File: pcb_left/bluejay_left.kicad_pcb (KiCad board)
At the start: 2 copper layers, 0 parts

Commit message: Work on PCBs
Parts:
- added C1: 22p, BlueJay footprints:C_Disc_D3.0mm_W1.6mm_P2.50mm, F.Cu at (191.0, 76.2)
- added C2: 22p, BlueJay footprints:C_Disc_D3.0mm_W1.6mm_P2.50mm, F.Cu at (191.0, 90.8)
- added C3: 4.7u, BlueJay footprints:CP_Radial_D4.0mm_P1.50mm, F.Cu at (201.8, 45.0)
- added C4: 100n, BlueJay footprints:C_Disc_D4.3mm_W1.9mm_P5.00mm, F.Cu at (193.2, 74.0)
- added C5: 100n, BlueJay footprints:C_Disc_D4.3mm_W1.9mm_P5.00mm, F.Cu at (206.8, 82.2)
- added DZ1: 3.6V, Diode_THT_AKL:D_DO-35_SOD27_P7.62mm_Horizontal_Zener, F.Cu at (167.0, 26.0)
- added DZ2: 3.6V, Diode_THT_AKL:D_DO-35_SOD27_P7.62mm_Horizontal_Zener, F.Cu at (172.8, 26.1)
- added Da1: 1N4148, Diode_THT_AKL:D_DO-35_SOD27_P7.62mm_Horizontal, F.Cu at (203.4, 107.2)
- added Da2: 1N4148, Diode_THT_AKL:D_DO-35_SOD27_P7.62mm_Horizontal, F.Cu at (203.4, 114.3)
- added Da3: 1N4148, Diode_THT_AKL:D_DO-35_SOD27_P7.62mm_Horizontal, F.Cu at (196.2, 140.5)
- added Da4: 1N4148, Diode_THT_AKL:D_DO-35_SOD27_P7.62mm_Horizontal, F.Cu at (203.4, 121.4)
- added Da5: 1N4148, Diode_THT_AKL:D_DO-35_SOD27_P7.62mm_Horizontal, F.Cu at (203.4, 133.3)
- added Db1: 1N4148, Diode_THT_AKL:D_DO-35_SOD27_P7.62mm_Horizontal, F.Cu at (191.5, 121.4)
- added Db2: 1N4148, Diode_THT_AKL:D_DO-35_SOD27_P7.62mm_Horizontal, F.Cu at (191.5, 114.3)
- added Db3: 1N4148, Diode_THT_AKL:D_DO-35_SOD27_P7.62mm_Horizontal, F.Cu at (191.5, 107.2)
- added Db4: 1N4148, Diode_THT_AKL:D_DO-35_SOD27_P7.62mm_Horizontal, F.Cu at (193.8, 126.2)
- added Db5: 1N4148, Diode_THT_AKL:D_DO-35_SOD27_P7.62mm_Horizontal, F.Cu at (191.5, 131.0)
- added Dc1: 1N4148, Diode_THT_AKL:D_DO-35_SOD27_P7.62mm_Horizontal, F.Cu at (179.5, 114.3)
- added Dc2: 1N4148, Diode_THT_AKL:D_DO-35_SOD27_P7.62mm_Horizontal, F.Cu at (181.9, 107.2)
- added Dc3: 1N4148, Diode_THT_AKL:D_DO-35_SOD27_P7.62mm_Horizontal, F.Cu at (179.5, 121.4)
- added Dc4: 1N4148, Diode_THT_AKL:D_DO-35_SOD27_P7.62mm_Horizontal, F.Cu at (181.9, 102.4)
- added Dc5: 1N4148, Diode_THT_AKL:D_DO-35_SOD27_P7.62mm_Horizontal, F.Cu at (179.5, 128.6)
- added Dd1: 1N4148, Diode_THT_AKL:D_DO-35_SOD27_P7.62mm_Horizontal, F.Cu at (108.1, 31.0)
- added Dd2: 1N4148, Diode_THT_AKL:D_DO-35_SOD27_P7.62mm_Horizontal, F.Cu at (117.6, 19.1)
- added Dd3: 1N4148, Diode_THT_AKL:D_DO-35_SOD27_P7.62mm_Horizontal, F.Cu at (108.1, 26.2)
- added Dd4: 1N4148, Diode_THT_AKL:D_DO-35_SOD27_P7.62mm_Horizontal, F.Cu at (105.7, 21.4)
- added Dd5: 1N4148, Diode_THT_AKL:D_DO-35_SOD27_P7.62mm_Horizontal, F.Cu at (105.4, 14.3)
- added De1: 1N4148, Diode_THT_AKL:D_DO-35_SOD27_P7.62mm_Horizontal, F.Cu at (89.1, 42.9)
- added De2: 1N4148, Diode_THT_AKL:D_DO-35_SOD27_P7.62mm_Horizontal, F.Cu at (89.1, 35.7)
- added De3: 1N4148, Diode_THT_AKL:D_DO-35_SOD27_P7.62mm_Horizontal, F.Cu at (91.4, 31.0)
- added De4: 1N4148, Diode_THT_AKL:D_DO-35_SOD27_P7.62mm_Horizontal, F.Cu at (91.4, 23.8)
- added Df2: 1N4148, Diode_THT_AKL:D_DO-35_SOD27_P7.62mm_Horizontal, F.Cu at (70.0, 52.4)
- added Df3: 1N4148, Diode_THT_AKL:D_DO-35_SOD27_P7.62mm_Horizontal, F.Cu at (70.0, 42.9)
- added Df4: 1N4148, Diode_THT_AKL:D_DO-35_SOD27_P7.62mm_Horizontal, F.Cu at (70.0, 35.7)
- added F1: 100mA, BlueJay footprints:polyfuse_5.1mm, F.Cu at (204.0, 35.7)
- added J1: SJ-43514, BlueJay footprints:CUI_SJ-43514, F.Cu at (195.3, 23.8)
- added PB1: RESET, BlueJay footprints:SW_PUSH_6mm, F.Cu at (149.0, 19.0)
- added PB2: BOOT, BlueJay footprints:SW_PUSH_6mm, F.Cu at (137.0, 19.0)
- added R1: 1.5k, BlueJay footprints:R_Axial_DIN0204_L3.6mm_D1.6mm_P5.08mm_Horizontal, F.Cu at (200.5, 55.8)
- added R2: 75R, BlueJay footprints:R_Axial_DIN0204_L3.6mm_D1.6mm_P5.08mm_Horizontal, F.Cu at (191.2, 55.7)
- added R3: 75R, BlueJay footprints:R_Axial_DIN0204_L3.6mm_D1.6mm_P5.08mm_Horizontal, F.Cu at (196.0, 55.7)
- added R4: 10k, BlueJay footprints:R_Axial_DIN0204_L3.6mm_D1.6mm_P5.08mm_Horizontal, F.Cu at (161.5, 23.5)
- added SWa1: KEYSW, BlueJay footprints:Kailh_socket_MX, F.Cu at (169.1, 47.6)
- added SWa2: KEYSW, BlueJay footprints:Kailh_socket_MX, F.Cu at (169.1, 66.7)
- added SWa3: KEYSW, BlueJay footprints:Kailh_socket_MX, F.Cu at (169.1, 85.7)
- added SWa4: KEYSW, BlueJay footprints:Kailh_socket_MX, F.Cu at (169.1, 104.8)
- added SWa5: KEYSW, BlueJay footprints:Kailh_socket_MX, F.Cu at (198.2, 154.4)
- added SWb1: KEYSW, BlueJay footprints:Kailh_socket_MX, F.Cu at (150.0, 45.2)
- added SWb2: KEYSW, BlueJay footprints:Kailh_socket_MX, F.Cu at (150.0, 64.3)
- added SWb3: KEYSW, BlueJay footprints:Kailh_socket_MX, F.Cu at (150.0, 83.3)
- added SWb4: KEYSW, BlueJay footprints:Kailh_socket_MX, F.Cu at (150.0, 102.4)
- added SWb5: KEYSW, BlueJay footprints:Kailh_socket_MX, F.Cu at (181.3, 141.2)
- added SWc1: KEYSW, BlueJay footprints:Kailh_socket_MX, F.Cu at (131.0, 38.1)
- added SWc2: KEYSW, BlueJay footprints:Kailh_socket_MX, F.Cu at (131.0, 57.1)
- added SWc3: KEYSW, BlueJay footprints:Kailh_socket_MX, F.Cu at (130.7, 76.2)
- added SWc4: KEYSW, BlueJay footprints:Kailh_socket_MX, F.Cu at (131.0, 95.2)
- added SWc5: KEYSW, BlueJay footprints:Kailh_socket_MX, F.Cu at (161.7, 132.4)
- added SWd1: KEYSW, BlueJay footprints:Kailh_socket_MX, F.Cu at (111.9, 45.2)
- added SWd2: KEYSW, BlueJay footprints:Kailh_socket_MX, F.Cu at (111.9, 64.3)
- added SWd3: KEYSW, BlueJay footprints:Kailh_socket_MX, F.Cu at (111.9, 83.3)
- added SWd4: KEYSW, BlueJay footprints:Kailh_socket_MX, F.Cu at (111.9, 102.4)
- added SWd5: KEYSW, BlueJay footprints:Kailh_socket_MX, F.Cu at (140.5, 128.6)
- added SWe1: KEYSW, BlueJay footprints:Kailh_socket_MX, F.Cu at (92.9, 52.4)
- added SWe2: KEYSW, BlueJay footprints:Kailh_socket_MX, F.Cu at (92.9, 71.4)
- added SWe3: KEYSW, BlueJay footprints:Kailh_socket_MX, F.Cu at (92.9, 90.5)
- added SWe4: KEYSW, BlueJay footprints:Kailh_socket_MX, F.Cu at (92.7, 109.9)
- added SWf2: KEYSW, BlueJay footprints:Kailh_socket_MX, F.Cu at (73.5, 71.4)
- added SWf3: KEYSW, BlueJay footprints:Kailh_socket_MX, F.Cu at (73.8, 90.5)
- added SWf4: KEYSW, BlueJay footprints:Kailh_socket_MX, F.Cu at (73.8, 109.5)
- added U1: ATmega328P-PU, Package_DIP_AKL:DIP-28_W7.62mm_Socket, F.Cu at (196.2, 62.1)
- added USB1: USB_B_Mini, BlueJay footprints:USB_Mini_B_Female_548190519, F.Cu at (181.0, 27.5)
- added Y1: 16MHz, BlueJay footprints:Crystal_HC49-4H_Vertical, F.Cu at (191.8, 86.0)
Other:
- board outline added: 17.2 x 1.3 mm

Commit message: Further work on pcbs
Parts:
- DZ1, DZ2: footprint Diode_THT_AKL:D_DO-35_SOD27_P7.62mm_Horizontal_Zener -> BlueJay footprints:D_DO-35_SOD27_P5.08mm_Horizontal
- Da1, Da2, Da3, Da4, Da5, Db1, Db2, Db3, Db4, Db5, Dc1, Dc2, Dc3, Dc4, Dc5, Dd1, Dd2, Dd3, Dd4, Dd5, De1, De2, De3, De4, Df2, Df3, Df4: footprint Diode_THT_AKL:D_DO-35_SOD27_P7.62mm_Horizontal -> BlueJay footprints:D_DO-35_SOD27_P5.08mm_Horizontal
- moved Df4 19.0 mm to (77.3, 53.2), turned to 180 degrees
- moved Df3 16.5 mm to (78.6, 57.0), turned to 180 degrees
- moved Df2 13.3 mm to (80.3, 60.8), turned to 180 degrees
- moved Dd2 12.7 mm to (117.1, 31.8), turned to 180 degrees
- moved De4 11.3 mm to (96.2, 34.0), turned to 180 degrees
- moved Dd1 10.6 mm to (117.8, 35.2), turned to 180 degrees
- moved De1 10.5 mm to (99.6, 42.2), turned to 180 degrees
- moved De2 9.94 mm to (98.2, 39.5), turned to 180 degrees
- moved De3 8.21 mm to (97.2, 36.8), turned to 180 degrees
- turned Dd3 to 180 degrees
- turned Dd4 to 180 degrees
- turned Dd5 to 180 degrees

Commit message: Further PCB updates
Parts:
- moved Dc4 30.0 mm to (207.1, 118.8), turned to 180 degrees
- moved Dc3 27.7 mm to (206.3, 114.2), turned to 180 degrees
- moved Dc1 25.2 mm to (203.1, 105.2), turned to 180 degrees
- moved Da3 24.6 mm to (188.8, 117.0), turned to 180 degrees
- moved Dc2 22.8 mm to (204.6, 109.8), turned to 180 degrees
- moved Da1 18.4 mm to (185.1, 109.5), turned to 180 degrees
- moved Dd5 17.2 mm to (108.1, 31.2)
- moved Da2 16.8 mm to (186.6, 113.0), turned to 180 degrees
- moved Db1 16.5 mm to (192.3, 105.0), turned to 180 degrees
- moved Dd4 13.9 mm to (109.8, 34.8)
- moved C3 13.4 mm to (190.0, 51.5)
- moved Dc5 12.7 mm to (191.8, 125.2), turned to 180 degrees
- moved Da4 12.5 mm to (190.8, 121.0), turned to 180 degrees
- moved Da5 12.5 mm to (199.3, 121.5), turned to 180 degrees
- moved F1 11.9 mm to (196.0, 44.5)
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
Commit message: Further work on pcbs
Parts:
- F1: footprint BlueJay footprints:polyfuse_5.1mm -> Fuse_AKL:Fuse_Bourns_MF-RG300
- SWa1, SWa2, SWa3, SWa4, SWa5, SWb1, SWb2, SWb3, SWb4, SWb5, SWc1, SWc2, SWc3, SWc4, SWc5, SWd1, SWd2, SWd3, SWd4, SWd5, SWe1, SWe2, SWe3, SWe4, SWf2, SWf3, SWf4: footprint BlueJay footprints:Kailh_socket_MX -> BlueJay footprints:SW_MX
- moved Da1 55.5 mm to (186.6, 54.0)
- moved Da2 45.5 mm to (186.6, 67.5)
- moved Da3 31.4 mm to (186.1, 85.8)
- moved Da4 22.0 mm to (186.1, 99.5)
- moved Da5 21.8 mm to (208.6, 141.2)
- moved De4 15.8 mm to (80.3, 31.0)
- moved C3 15.6 mm to (203.5, 43.8)
- moved De3 15.1 mm to (82.8, 36.8)
- moved De2 14.8 mm to (84.8, 42.0)
- moved Dd4 14.5 mm to (95.3, 35.2)
- moved Dd5 14.3 mm to (93.8, 30.2)
- moved Dc4 13.1 mm to (205.5, 131.8)
- moved Dd2 12.2 mm to (106.3, 34.0)
- moved R2 11.0 mm to (195.0, 55.0)
- moved U1 11.0 mm to (195.9, 58.3)
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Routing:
- added copper zone on B.Cu, net GND
- added copper zone on F.Cu, net GND
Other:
- board size 17.2 x 1.3 mm -> 147 x 141 mm

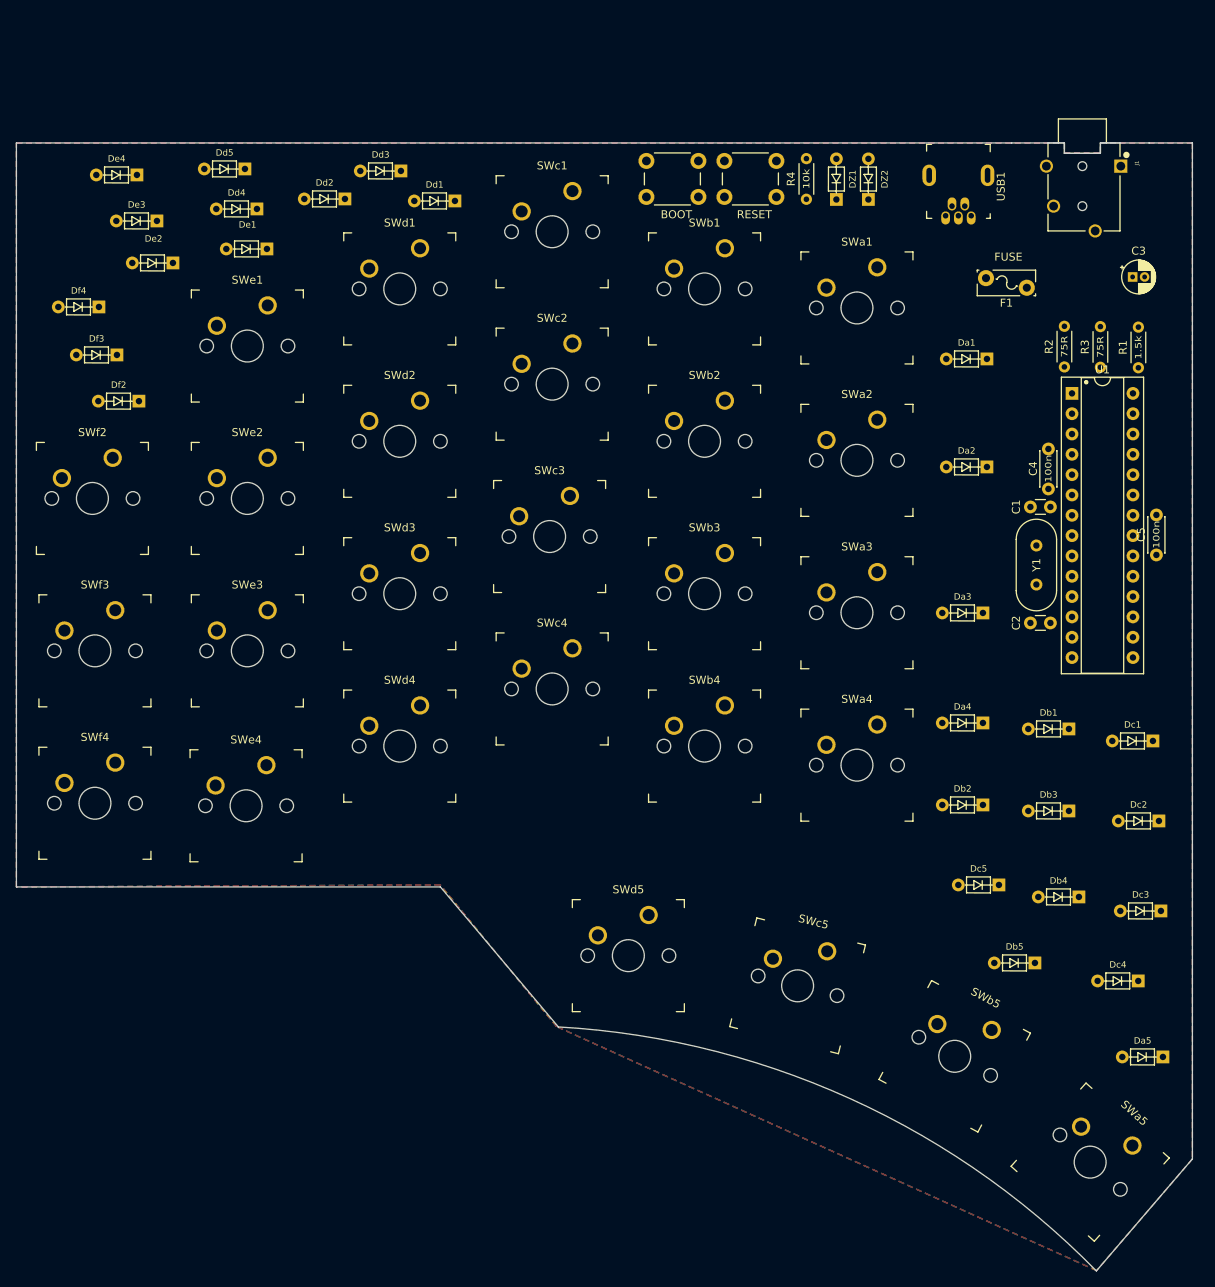
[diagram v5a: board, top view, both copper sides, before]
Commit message: Preliminary routing left hand pcb
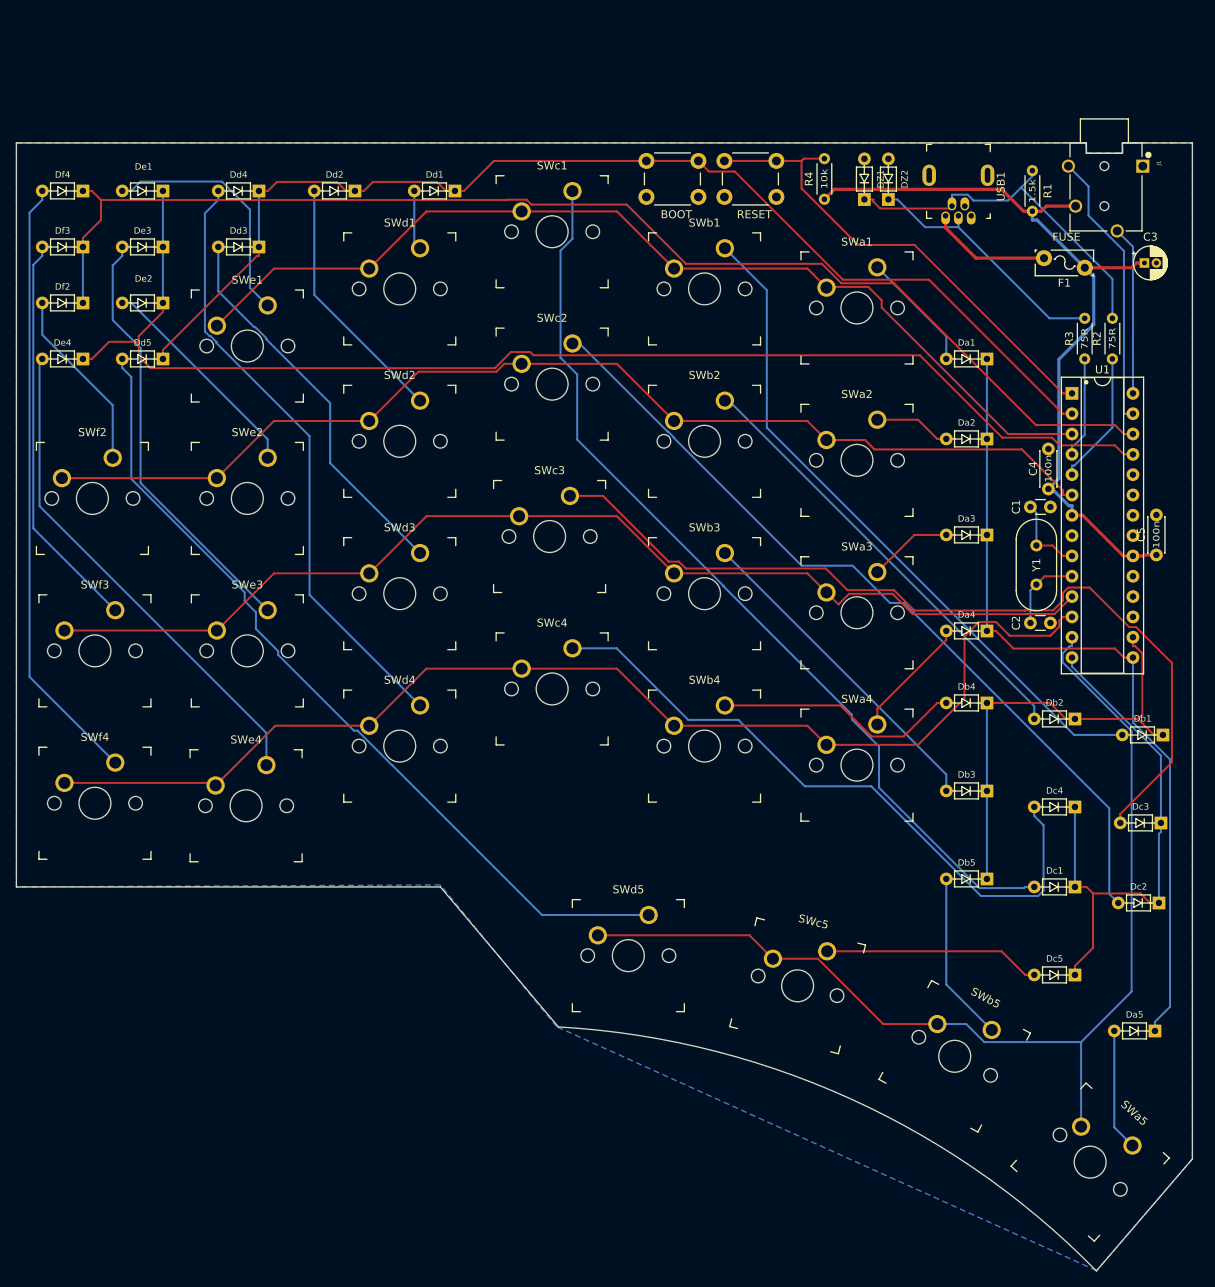
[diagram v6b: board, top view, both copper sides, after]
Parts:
- moved R1 28.0 mm to (191.0, 30.5), turned to -90 degrees
- moved Db4 26.8 mm to (186.6, 97.0)
- moved Dd5 25.9 mm to (83.6, 54.0)
- moved De4 24.0 mm to (73.6, 54.0)
- moved Dc4 23.1 mm to (197.6, 110.0)
- moved Dc1 20.7 mm to (197.6, 120.0)
- moved Dd3 20.1 mm to (95.6, 40.0)
- moved Db2 15.7 mm to (197.6, 99.0)
- moved De1 14.9 mm to (83.6, 33.0)
- moved Dc5 14.7 mm to (197.6, 131.0)
- moved Df4 14.6 mm to (73.6, 33.0)
- moved Df3 14.2 mm to (73.6, 40.0)
- moved Df2 14.1 mm to (73.6, 47.0)
- moved Db5 12.1 mm to (186.6, 119.0)
- moved Db1 11.8 mm to (208.6, 101.0)
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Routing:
- net /colE: track 0.00 -> 160.8 mm
- net /colF: track 0.00 -> 157.7 mm
- net /row4: track 0.00 -> 149.1 mm
- net /colD: track 0.00 -> 144.3 mm
- net /row2: track 0.00 -> 139.3 mm
- net /row3: track 0.00 -> 138.9 mm
- net /row5: track 0.00 -> 134.0 mm
- net /row1: track 0.00 -> 124.9 mm
- net Net-(Dc1-Pad2): track 0.00 -> 116.3 mm
- net Net-(Dc3-Pad2): track 0.00 -> 109.5 mm
- net Net-(Dd5-Pad2): track 0.00 -> 104.8 mm
- net Net-(Dc2-Pad2): track 0.00 -> 103.5 mm
- net /colA: track 0.00 -> 103.0 mm
- net VCC: track 0.00 -> 99.2 mm
- net Net-(Db1-Pad2): track 0.00 -> 84.9 mm
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- removed copper zone on F.Cu, net GND
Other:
- outline, holes or cut-outs redrawn

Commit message: Tweaks to component placements - left hand
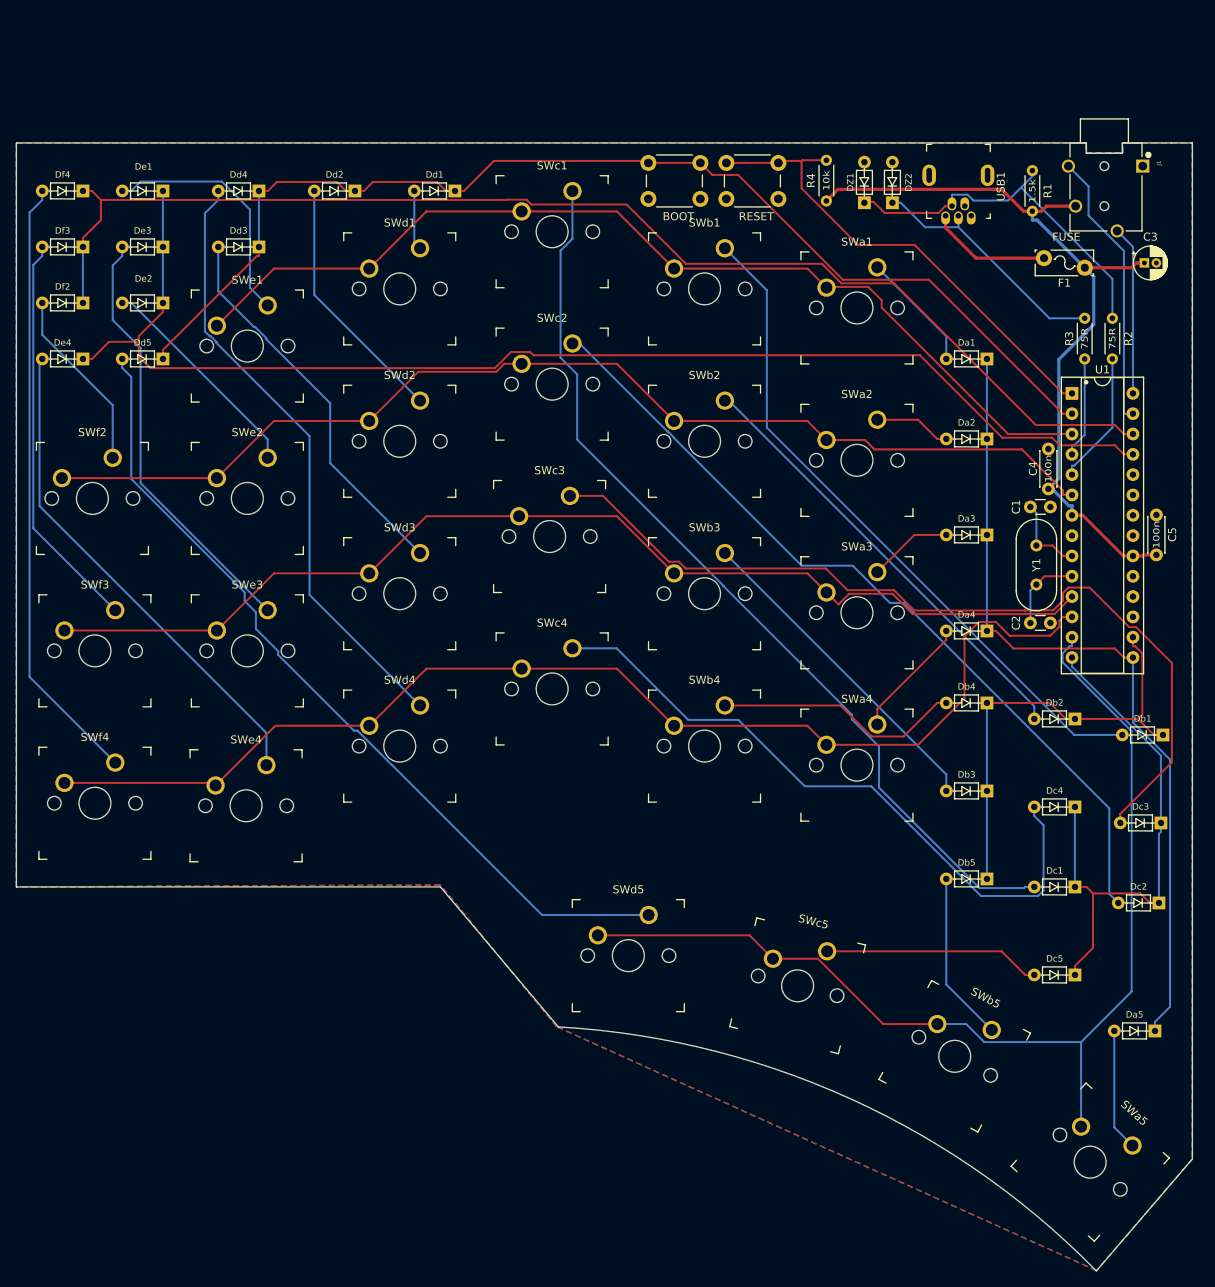
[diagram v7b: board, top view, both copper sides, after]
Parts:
- moved DZ2 0.65 mm to (173.5, 35.8)
- moved DZ1 0.41 mm to (170.0, 35.8)
- moved PB1 0.35 mm to (152.8, 29.5)
- moved PB2 0.35 mm to (143.0, 29.5)
- moved R4 0.33 mm to (165.2, 34.2)
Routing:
- net Net-(DZ2-Pad1): track 32.1 -> 31.4 mm
- added copper zone on F.Cu, net GND
